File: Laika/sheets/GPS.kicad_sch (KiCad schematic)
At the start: 0 parts

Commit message: Minimal schematic for U-Blox SAM-M8Q module
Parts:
- added R28, R29: 0, symbol Device:R
- added U6: SAM-M8Q, RF_GPS:ublox_SAM-M8Q, symbol RF_GPS:SAM-M8Q
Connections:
- new net: R29.1, U6.13 (TXD)
- new net: R28.1, U6.14 (RXD)
- new net GND: U6.1 (GND), U6.10 (GND), U6.11 (GND), U6.15 (GND), U6.16 (GND), U6.20 (GND), U6.4 (GND), U6.5 (GND), U6.6 (GND)
- new net UBLOX_POWER: U6.17 (VCC), U6.2 (VCC_IO), U6.3 (V_BCKP)
- new net UBLOX_PPS: U6.7 (TIMEPULSE)
- new net UBLOX_RESET: U6.18 (~{RESET})
- new net UBLOX_RX: R28.2
- new net UBLOX_TX: R29.2
- no-connect marks 0 -> 4
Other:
- note added: "GPS"
- note added: "GPS Module"
- note added: "Optional EMI protection resistors Choose a value R > 20ohm Follow section 3.3 of HW Integration Guide"
- note added: "The M8Q is NRND. However it is plentiful in stock. The chip is pin-compatible with the M10Q"

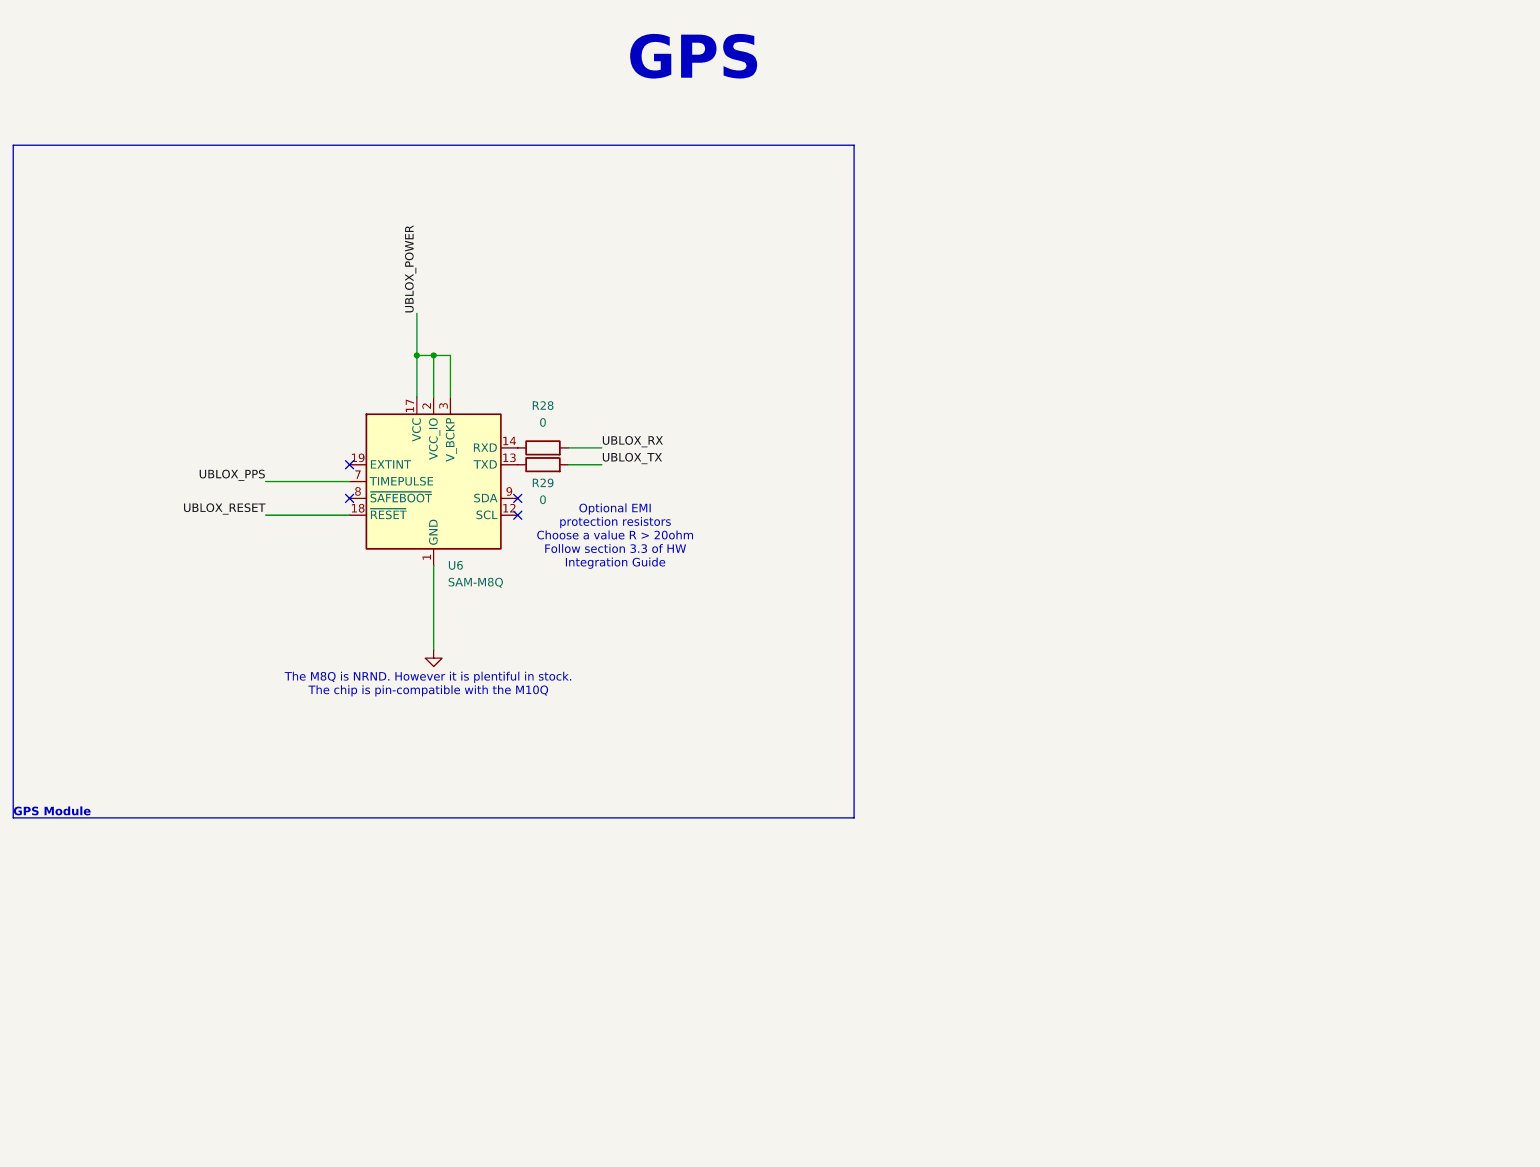
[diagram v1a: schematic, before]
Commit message: Added schematic for selecting between onboard GPS and external GPS
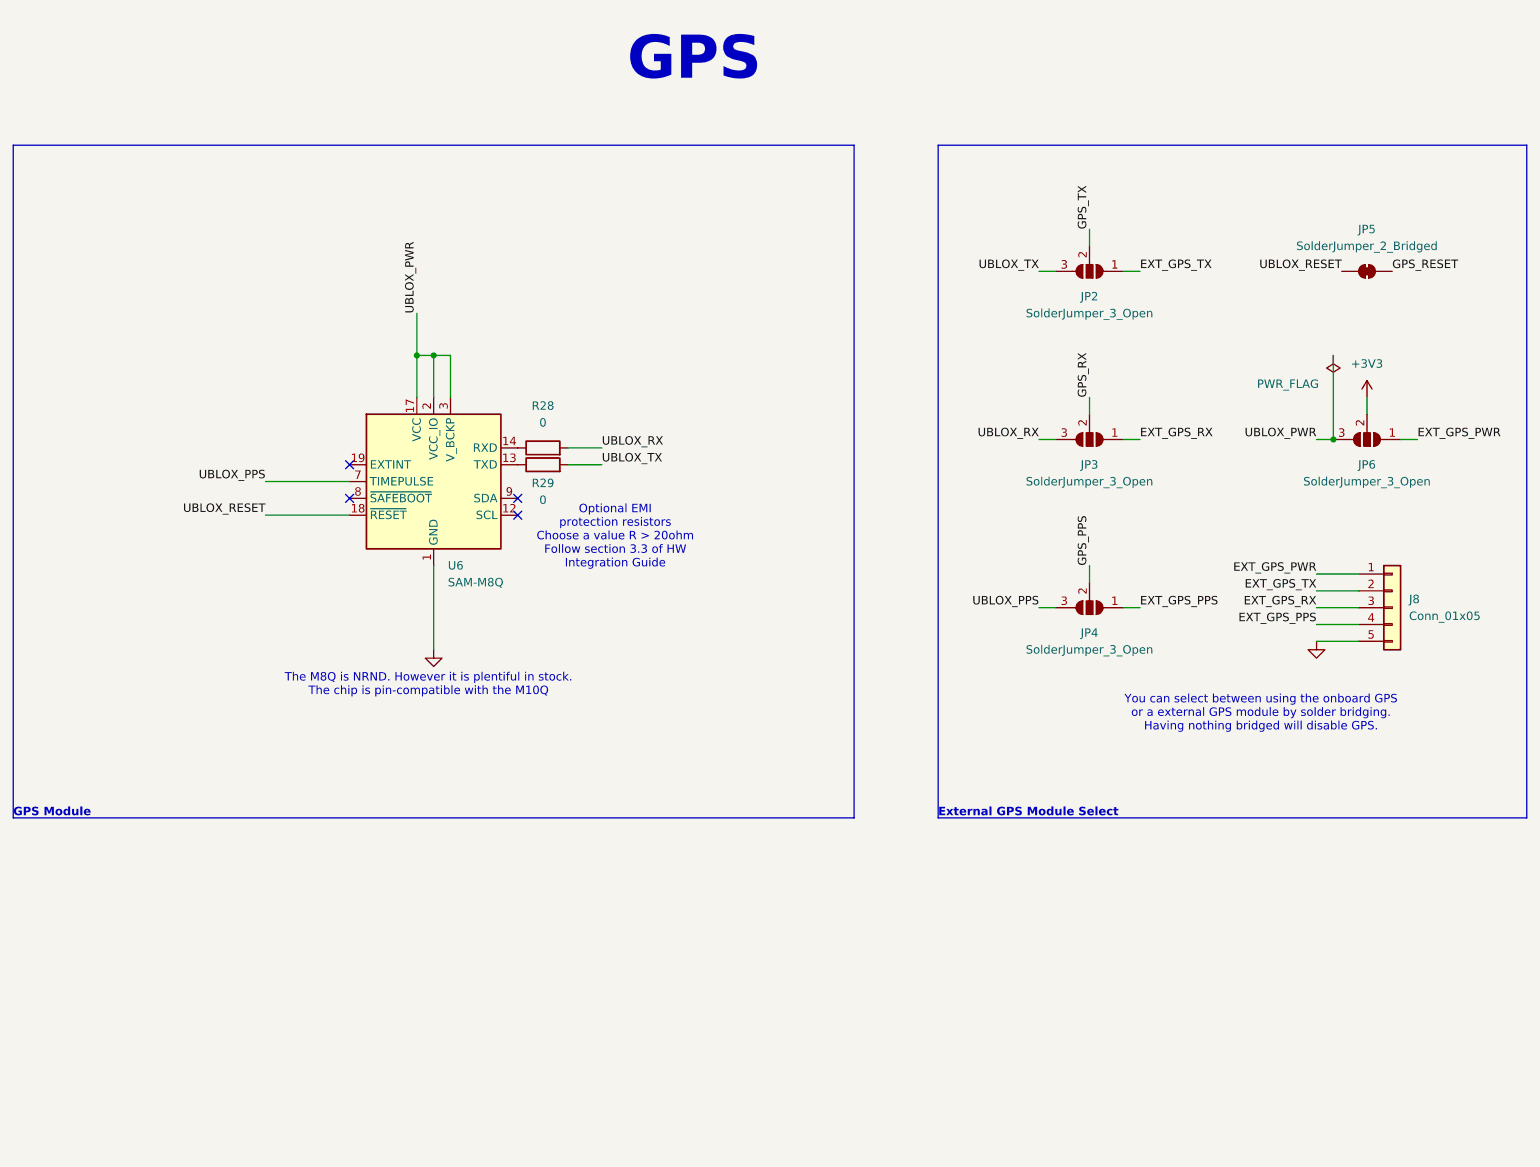
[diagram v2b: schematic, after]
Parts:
- added J8: Conn_01x05, symbol Connector_Generic:Conn_01x05
- added JP2, JP3, JP4, JP6: SolderJumper_3_Open, Jumper:SolderJumper-3_P1.3mm_Open_Pad1.0x1.5mm, symbol Jumper:SolderJumper_3_Open
- added JP5: SolderJumper_2_Bridged, Jumper:SolderJumper-2_P1.3mm_Bridged_Pad1.0x1.5mm, symbol Jumper:SolderJumper_2_Bridged
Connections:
- net GND: now also J8.5 (Pin_5)
- net UBLOX_PPS: now also JP4.3 (B)
- net UBLOX_RESET: now also JP5.1 (A)
- net UBLOX_RX: now also JP3.3 (B)
- net UBLOX_TX: now also JP2.3 (B)
- net UBLOX_POWER renamed UBLOX_PWR
- net UBLOX_PWR: now also JP6.3 (B)
- new net +3V3: JP6.2 (C)
- new net EXT_GPS_PPS: J8.4 (Pin_4), JP4.1 (A)
- new net EXT_GPS_PWR: J8.1 (Pin_1), JP6.1 (A)
- new net EXT_GPS_RX: J8.3 (Pin_3), JP3.1 (A)
- new net EXT_GPS_TX: J8.2 (Pin_2), JP2.1 (A)
- new net GPS_PPS: JP4.2 (C)
- new net GPS_RESET: JP5.2 (B)
- new net GPS_RX: JP3.2 (C)
- new net GPS_TX: JP2.2 (C)
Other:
- note added: "External GPS Module Select"
- note added: "You can select between using the onboard GPS or a external GPS module by solder bridging. Having nothing bridged will disable GPS."

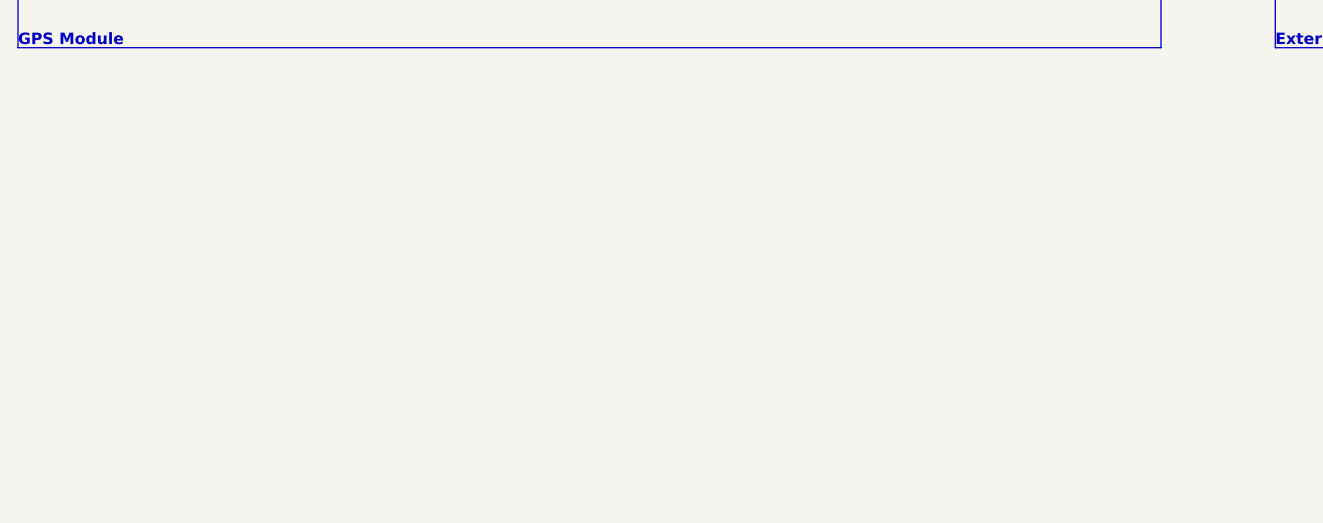
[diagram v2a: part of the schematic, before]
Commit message: Connected GPS to UART2.
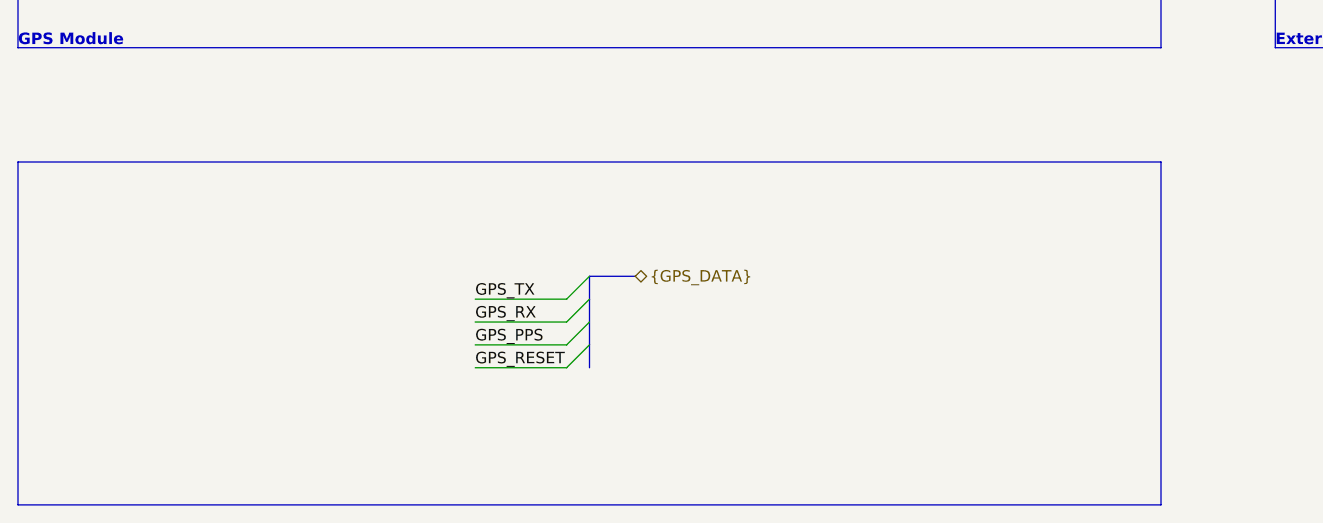
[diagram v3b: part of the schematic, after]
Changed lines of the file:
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@@
 		(comment 1 "${VARIANT}")
+	)
+	(bus_alias "GPS_DATA"
+		(members "GPS_TX" "GPS_RX" "GPS_PPS" "GPS_RESET")
 	)
 	(rectangle
@@
 		(start 177.8 38.1)
 		(end 266.7 139.7)
+		(stroke
+			(width 0)
+			(type default)
+		)
+		(fill
+			(type none)
+		)
+	)
+	(rectangle
+		(start 38.1 152.4)
+		(end 165.1 190.5)
 		(stroke
 			(width 0)
@@
 		(at 114.3 93.98)
 	)
+	(bus_entry
+		(at 101.6 170.18)
+		(size -2.54 2.54)
+		(stroke
+			(width 0)
+			(type default)
+		)
+	)
+	(bus_entry
+		(at 101.6 172.72)
+		(size -2.54 2.54)
+		(stroke
+			(width 0)
+			(type default)
+		)
+	)
+	(bus_entry
+		(at 101.6 165.1)
+		(size -2.54 2.54)
+		(stroke
+			(width 0)
+			(type default)
+		)
+	)
+	(bus_entry
+		(at 101.6 167.64)
+		(size -2.54 2.54)
+		(stroke
+			(width 0)
+			(type default)
+		)
+	)
 	(wire
 		(pts
@@
 	(wire
 		(pts
+			(xy 88.9 167.64) (xy 99.06 167.64)
+		)
+		(stroke
+			(width 0)
+			(type default)
+		)
+	)
+	(wire
+		(pts
 			(xy 101.6 114.3) (xy 101.6 101.6)
 		)
@@
 		)
 	)
+	(bus
+		(pts
+			(xy 101.6 167.64) (xy 101.6 170.18)
+		)
+		(stroke
+			(width 0)
+			(type default)
+		)
+	)
 	(wire
 		(pts
@@
 		)
 	)
+	(bus
+		(pts
+			(xy 106.68 165.1) (xy 101.6 165.1)
+		)
+		(stroke
+			(width 0)
+			(type default)
+		)
+	)
+	(bus
+		(pts
+			(xy 101.6 172.72) (xy 101.6 175.26)
+		)
+		(stroke
+			(width 0)
+			(type default)
+		)
+	)
 	(wire
 		(pts
@@
 		)
 	)
+	(bus
+		(pts
+			(xy 101.6 165.1) (xy 101.6 167.64)
+		)
+		(stroke
+			(width 0)
+			(type default)
+		)
+	)
 	(wire
 		(pts
@@
 	(wire
 		(pts
+			(xy 88.9 175.26) (xy 99.06 175.26)
+		)
+		(stroke
+			(width 0)
+			(type default)
+		)
+	)
+	(wire
+		(pts
 			(xy 193.04 82.55) (xy 195.58 82.55)
 		)
@@
 	(wire
 		(pts
+			(xy 88.9 170.18) (xy 99.06 170.18)
+		)
+		(stroke
+			(width 0)
+			(type default)
+		)
+	)
+	(wire
+		(pts
 			(xy 234.95 105.41) (xy 241.3 105.41)
 		)
@@
 		)
 	)
+	(bus
+		(pts
+			(xy 101.6 170.18) (xy 101.6 172.72)
+		)
+		(stroke
+			(width 0)
+			(type default)
+		)
+	)
 	(wire
 		(pts
 			(xy 99.06 69.85) (xy 99.06 76.2)
+		)
+		(stroke
+			(width 0)
+			(type default)
+		)
+	)
+	(wire
+		(pts
+			(xy 88.9 172.72) (xy 99.06 172.72)
 		)
 		(stroke
@@
 		)
 	)
+	(label "GPS_PPS"
+		(at 88.9 172.72 0)
+		(effects
+			(font
+				(size 1.27 1.27)
+			)
+			(justify left bottom)
+		)
+	)
 	(label "EXT_GPS_TX"
 		(at 208.28 57.15 0)
@@
 		)
 	)
+	(label "GPS_TX"
+		(at 88.9 167.64 0)
+		(effects
+			(font
+				(size 1.27 1.27)
+			)
+			(justify left bottom)
+		)
+	)
+	(label "GPS_RESET"
+		(at 88.9 175.26 0)
+		(effects
+			(font
+				(size 1.27 1.27)
+			)
+			(justify left bottom)
+		)
+	)
 	(label "EXT_GPS_RX"
 		(at 208.28 82.55 0)
@@
 		)
 	)
+	(label "GPS_RX"
+		(at 88.9 170.18 0)
+		(effects
+			(font
+				(size 1.27 1.27)
+			)
+			(justify left bottom)
+		)
+	)
 	(label "EXT_GPS_RX"
 		(at 234.95 107.95 180)
@@
 		)
 	)
+	(hierarchical_label "{GPS_DATA}"
+		(shape bidirectional)
+		(at 106.68 165.1 0)
+		(effects
+			(font
+				(size 1.27 1.27)
+			)
+			(justify left)
+		)
+	)

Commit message: Revert "GPS"
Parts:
- removed J8: Conn_01x05, symbol Connector_Generic:Conn_01x05
- removed JP2, JP3, JP4, JP6: SolderJumper_3_Open, Jumper:SolderJumper-3_P1.3mm_Open_Pad1.0x1.5mm, symbol Jumper:SolderJumper_3_Open
- removed JP5: SolderJumper_2_Bridged, Jumper:SolderJumper-2_P1.3mm_Bridged_Pad1.0x1.5mm, symbol Jumper:SolderJumper_2_Bridged
- removed R28, R29: 0, symbol Device:R
- removed U6: SAM-M8Q, RF_GPS:ublox_SAM-M8Q, symbol RF_GPS:SAM-M8Q
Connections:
- no-connect marks 4 -> 0
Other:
- note removed: "External GPS Module Select"
- note removed: "GPS"
- note removed: "GPS Module"
- note removed: "Optional EMI protection resistors Choose a value R > 20ohm Follow section 3.3 of HW Integration Guide"
- note removed: "The M8Q is NRND. However it is plentiful in stock. The chip is pin-compatible with the M10Q"
- note removed: "You can select between using the onboard GPS or a external GPS module by solder bridging. Having nothing bridged will disable GPS."
